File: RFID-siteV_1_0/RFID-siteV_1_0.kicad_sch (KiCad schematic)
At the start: 34 parts

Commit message: sch
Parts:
- removed R?: 1k, Resistor_SMD:R_0805_2012Metric, symbol Device:R
- added C4, C5, C6, C7: 0.1uF, Capacitor_SMD:C_0805_2012Metric, symbol Device:C
- added F1: Fuse 200mA, Fuse:Fuse_1206_3216Metric, symbol Device:Fuse
- added H1: (no value), symbol Mechanical:MountingHole
- added H2, H3, H4, H5, H6: MountingHole, MountingHole:MountingHole_2.5mm, symbol Mechanical:MountingHole
- added JP1: (no value), symbol Jumper:SolderJumper_3_Bridged12
- U2: renamed from U?; value (none) -> STM32L053R8Tx; footprint (none) -> Package_QFP:LQFP-64_10x10mm_P0.5mm
- U3: renamed from U?; value E22-400T22S -> (none)
- gave numbers to parts that had none: 31
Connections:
- net LoRa_RXD is gone; now on net L53R8_UART1_TX: JP4.2 (B)
- net LoRa_TXD is gone; now on net L53R8_UART1_RX: JP5.2 (B)
- net +3V3: now also C4.1, C5.1, C6.1, C7.1, JP1.3 (B)
- net +5V: now also F1.1; no longer J1.A4 (VBUS), J1.A9 (VBUS), J1.B4 (VBUS), J1.B9 (VBUS)
- net GND: now also C4.2, C5.2, C6.2, C7.2, JP1.1 (A)
- net LoRa_AUX: now also U2.41 (PA8)
- net PB0: now also U2.26 (PB0)
- net PB1: now also U2.27 (PB1)
- net PB2: now also U2.28 (PB2)
- net buz: now also U2.55 (PB3)
- net BOOT0: now reaches U2.60 (BOOT0)
- net BOOT0: now also JP1.2 (C)
- new net: F1.2, J1.A4 (VBUS), J1.A9 (VBUS), J1.B4 (VBUS), J1.B9 (VBUS)
- no-connect marks 3 -> 43

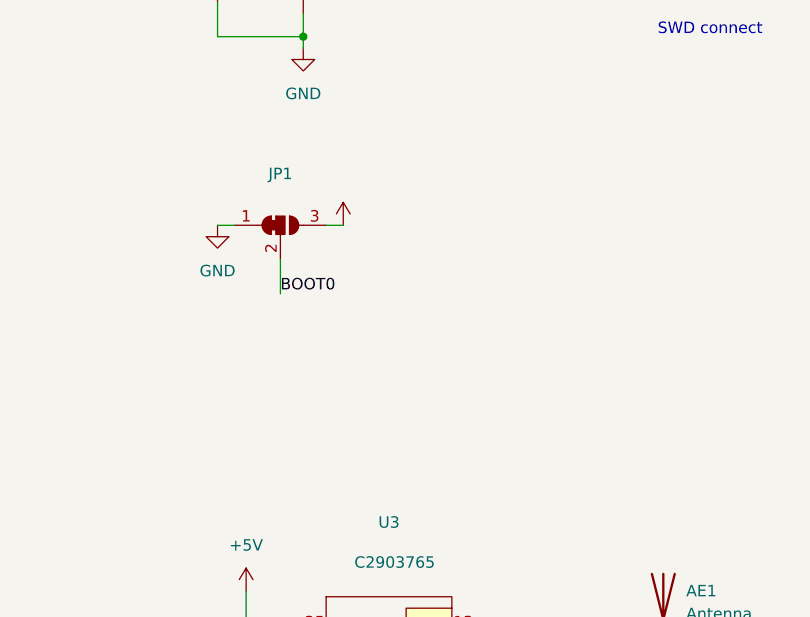
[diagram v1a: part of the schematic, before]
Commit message: Update RFID-siteV_1_0.kicad_sch
add boot 0 select pin
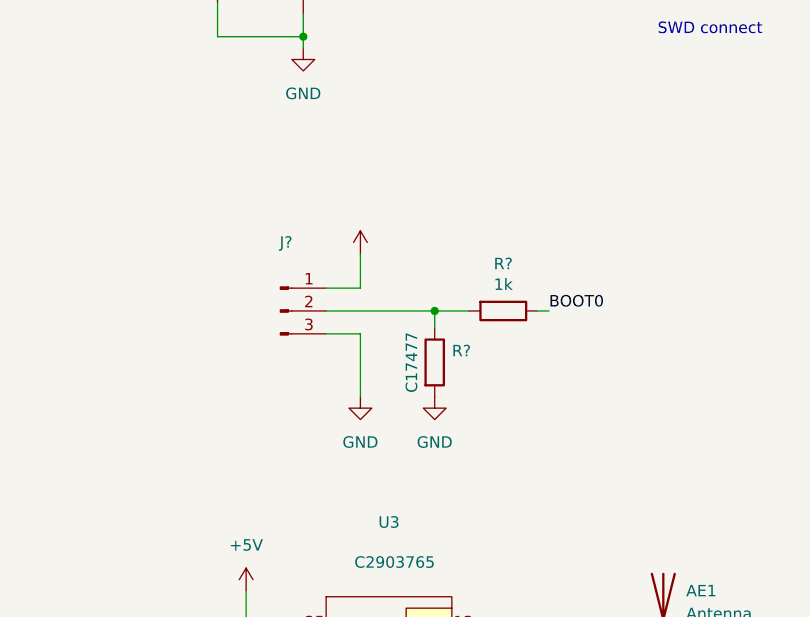
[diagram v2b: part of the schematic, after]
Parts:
- removed JP1: (no value), symbol Jumper:SolderJumper_3_Bridged12
- added J?: (no value), symbol Connector:Conn_01x03_Male
- added R?: (no value), symbol Device:R
- added R?: 1k, Resistor_SMD:R_0805_2012Metric, symbol Device:R
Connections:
- net +3V3: now also J?.1 (Pin_1)
- net BOOT0: now also R?.1
- net GND: now also J?.3 (Pin_3), R?.2
- new net: J?.2 (Pin_2), R?.1, R?.2

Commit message: Update RFID-siteV_1_0.kicad_sch
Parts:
- gave numbers to parts that had none: 3
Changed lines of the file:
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@@
   (symbol (lib_id "Device:R") (at 241.3 89.535 0) (unit 1)
     (in_bom yes) (on_board yes)
-    (property "Reference" "R?" (id 0) (at 243.205 88.2649 0)
+    (property "Reference" "R12" (id 0) (at 243.205 88.2649 0)
       (effects (font (size 1.27 1.27)) (justify left))
     )
@@
   (symbol (lib_id "Connector:Conn_01x03_Male") (at 224.155 83.82 0) (unit 1)
     (in_bom yes) (on_board yes) (fields_autoplaced)
-    (property "Reference" "J?" (id 0) (at 224.79 76.2 0))
+    (property "Reference" "J4" (id 0) (at 224.79 76.2 0))
     (property "Value" "" (id 1) (at 224.79 78.74 0))
     (property "Footprint" "" (id 2) (at 224.155 83.82 0)
@@
   (symbol (lib_id "Device:R") (at 248.92 83.82 270) (unit 1)
     (in_bom yes) (on_board yes)
-    (property "Reference" "R?" (id 0) (at 248.92 78.5938 90))
+    (property "Reference" "R13" (id 0) (at 248.92 78.5938 90))
     (property "Value" "1k" (id 1) (at 248.92 80.893 90))
     (property "Footprint" "Resistor_SMD:R_0805_2012Metric" (id 2) (at 248.92 82.042 90)
@@
   (symbol (lib_id "power:GND") (at 241.3 93.345 0) (unit 1)
     (in_bom yes) (on_board yes) (fields_autoplaced)
-    (property "Reference" "#PWR?" (id 0) (at 241.3 99.695 0)
+    (property "Reference" "#PWR032" (id 0) (at 241.3 99.695 0)
       (effects (font (size 1.27 1.27)) hide)
     )
@@
     )
     (path "/ca7b8c55-e6e0-4112-a65a-eea1968b0666"
-      (reference "#PWR?") (unit 1) (value "GND") (footprint "")
+      (reference "#PWR032") (unit 1) (value "GND") (footprint "")
     )
     (path "/3ae1892a-0bb4-4f17-a391-4593a1c74cc5"
@@
     )
     (path "/b0455d33-0bf3-427e-a253-ef9caa588f5b"
-      (reference "J?") (unit 1) (value "Conn_01x03_Male") (footprint "Connector_PinHeader_2.54mm:PinHeader_1x03_P2.54mm_Vertical")
+      (reference "J4") (unit 1) (value "Conn_01x03_Male") (footprint "Connector_PinHeader_2.54mm:PinHeader_1x03_P2.54mm_Vertical")
     )
     (path "/d5e54d24-df8a-4528-9616-b9adfb60ae59"
@@
     )
     (path "/04b0422e-67f3-43c8-bd50-f4e69ba81876"
-      (reference "R?") (unit 1) (value "0R") (footprint "Resistor_SMD:R_0805_2012Metric")
+      (reference "R12") (unit 1) (value "0R") (footprint "Resistor_SMD:R_0805_2012Metric")
     )
     (path "/c22bdfb4-b53a-44db-a9b1-f00a19c4fefa"
-      (reference "R?") (unit 1) (value "1k") (footprint "Resistor_SMD:R_0805_2012Metric")
+      (reference "R13") (unit 1) (value "1k") (footprint "Resistor_SMD:R_0805_2012Metric")
     )
     (path "/fdd48cbc-c4f6-4e8d-b774-1cd02a92d89d"

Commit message: Update RFID-siteV_1_0.kicad_sch
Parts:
- J4: now left out of the parts list
- R13: value 1k -> (none); footprint Resistor_SMD:R_0805_2012Metric -> (none); LCSC (none) -> C17513
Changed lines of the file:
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@@
   )
   (symbol (lib_id "Connector:Conn_01x03_Male") (at 224.155 83.82 0) (unit 1)
-    (in_bom yes) (on_board yes) (fields_autoplaced)
+    (in_bom no) (on_board no) (fields_autoplaced)
     (property "Reference" "J4" (id 0) (at 224.79 76.2 0))
     (property "Value" "" (id 1) (at 224.79 78.74 0))
@@
     (in_bom yes) (on_board yes)
     (property "Reference" "R13" (id 0) (at 248.92 78.5938 90))
-    (property "Value" "1k" (id 1) (at 248.92 80.893 90))
-    (property "Footprint" "Resistor_SMD:R_0805_2012Metric" (id 2) (at 248.92 82.042 90)
+    (property "Value" "" (id 1) (at 248.92 80.893 90))
+    (property "Footprint" "" (id 2) (at 248.92 82.042 90)
       (effects (font (size 1.27 1.27)) hide)
     )
@@
       (effects (font (size 1.27 1.27)) hide)
     )
+    (property "LCSC" "C17513" (id 4) (at 248.92 83.82 90)
+      (effects (font (size 1.27 1.27)) hide)
+    )

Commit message: Update RFID-siteV_1_0.kicad_sch
SWD
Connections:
- net SWCLK: now also U2.49 (PA14)
- net SWDIO: now also U2.46 (PA13)
- no-connect marks 43 -> 41

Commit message: update
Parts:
- added C8: 0.1uF, Capacitor_SMD:C_0805_2012Metric, symbol Device:C
- renumbered C8 to C9, J4 to J3, J3 to J4, JP2 to JP1, JP3 to JP2, JP4 to JP3, JP5 to JP4
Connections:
- net +3V3: now also C8.1
- net GND: now also C8.2

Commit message: jlcpcb
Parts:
- Q1: LCSC C909754 -> C20526
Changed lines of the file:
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@@
       (effects (font (size 1.27 1.27)) (justify left) hide)
     )
-    (property "LCSC" "C909754" (id 4) (at 97.155 92.71 0))
+    (property "LCSC" "C20526" (id 4) (at 97.155 92.71 0))
     (pin "1")
     (pin "2")
